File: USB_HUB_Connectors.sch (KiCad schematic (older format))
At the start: 86 parts, among them IC4 AP22652W6-7, J10 E8124-015-01, J11 E8124-015-01, U15 USB57442G, Y2 ABM8G-25.000MHZ-B4Y-T

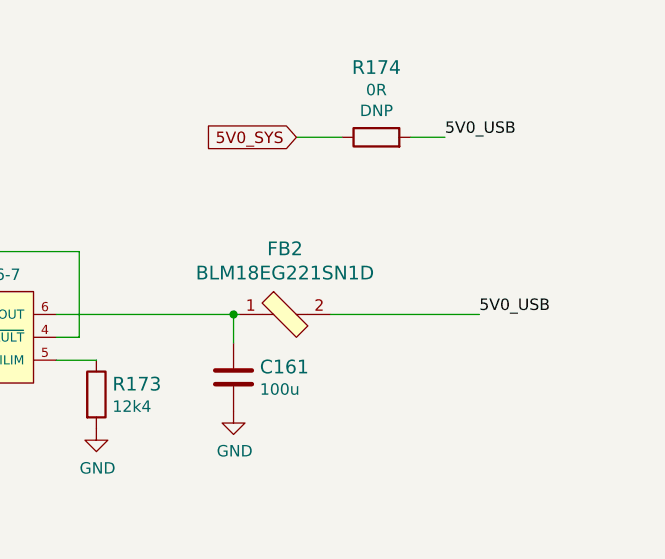
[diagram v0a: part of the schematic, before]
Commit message: Connecting LT9611
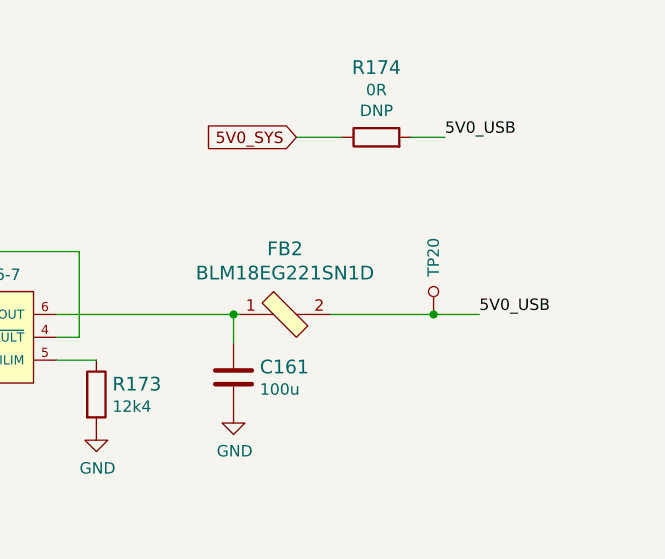
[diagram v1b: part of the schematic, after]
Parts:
- added TP20: TP_SMD_0_75MM, sc606-baseboard-footprints:Testpoint_smd_0_75mm, symbol sc606-baseboard:TP_SMD_0_75MM
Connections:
- net 5V0_USB: now also TP20.1
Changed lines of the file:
@@
 5V0_USB
 Wire Wire Line
-	15225 1925 14575 1925
+	15225 1925 15025 1925
 $Comp
 L sc606-baseboard:R_200k_0402 R?
@@
 P 12400 7400
 AR Path="/61F60810/620C24E5" Ref="#PWR?"  Part="1"
-AR Path="/63348E64/620C24E5" Ref="#PWR?"  Part="1"
-F 0 "#PWR?" H 12400 7150 50  0001 C CNN
+AR Path="/63348E64/620C24E5" Ref="#PWR0199"  Part="1"
+F 0 "#PWR0199" H 12400 7150 50  0001 C CNN
 F 1 "GND" H 12405 7227 50  0000 C CNN
 F 2 "" H 12400 7400 50  0001 C CNN
@@
 P 4550 8300
 AR Path="/61F60810/620CB62E" Ref="#PWR?"  Part="1"
-AR Path="/63348E64/620CB62E" Ref="#PWR?"  Part="1"
-F 0 "#PWR?" H 4550 8050 50  0001 C CNN
+AR Path="/63348E64/620CB62E" Ref="#PWR0200"  Part="1"
+F 0 "#PWR0200" H 4550 8050 50  0001 C CNN
 F 1 "GND" H 4555 8127 50  0000 C CNN
 F 2 "" H 4550 8300 50  0001 C CNN
@@
 	-1   0    0    -1
 $EndComp
+$Comp
+L sc606-baseboard:TP_SMD_0_75MM TP20
+U 1 1 621ACE00
+P 15025 1825
+F 0 "TP20" V 15025 1675 50  0000 C CNN
+F 1 "TP_SMD_0_75MM" H 15025 1725 50  0001 C CNN
+F 2 "sc606-baseboard-footprints:Testpoint_smd_0_75mm" H 15225 2025 60  0001 L CNN
+F 3 "" H 15225 2125 60  0001 L CNN
+	1    15025 1825
+	-1   0    0    1
+$EndComp
+Connection ~ 15025 1925
+Wire Wire Line
+	15025 1925 14575 1925
 $EndSCHEMATC

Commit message: Corrected power supplies. Change of TP to 1,5mm
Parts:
- TP18, TP19, TP20, TP23, TP24: value TP_SMD_0_75MM -> TP_SMD_1_5MM; footprint sc606-baseboard-footprints:Testpoint_smd_0_75mm -> sc606-baseboard-footprints:TP-R-1.5
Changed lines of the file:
@@
 P 11300 6600
 F 0 "TP23" V 11300 6450 50  0000 C CNN
-F 1 "TP_SMD_0_75MM" H 11300 6500 50  0001 C CNN
-F 2 "sc606-baseboard-footprints:Testpoint_smd_0_75mm" H 11500 6800 60  0001 L CNN
+F 1 "TP_SMD_1_5MM" H 11300 6500 50  0001 C CNN
+F 2 "sc606-baseboard-footprints:TP-R-1.5" H 11500 6800 60  0001 L CNN
 F 3 "" H 11500 6900 60  0001 L CNN
 	1    11300 6600
@@
 P 13200 6300
 F 0 "TP24" V 13200 6200 50  0000 C CNN
-F 1 "TP_SMD_0_75MM" H 13200 6200 50  0001 C CNN
-F 2 "sc606-baseboard-footprints:Testpoint_smd_0_75mm" H 13400 6500 60  0001 L CNN
+F 1 "TP_SMD_1_5MM" H 13200 6200 50  0001 C CNN
+F 2 "sc606-baseboard-footprints:TP-R-1.5" H 13400 6500 60  0001 L CNN
 F 3 "" H 13400 6600 60  0001 L CNN
 	1    13200 6300
@@
 P 3450 7500
 F 0 "TP18" V 3450 7350 50  0000 C CNN
-F 1 "TP_SMD_0_75MM" H 3450 7400 50  0001 C CNN
-F 2 "sc606-baseboard-footprints:Testpoint_smd_0_75mm" H 3650 7700 60  0001 L CNN
+F 1 "TP_SMD_1_5MM" H 3450 7400 50  0001 C CNN
+F 2 "sc606-baseboard-footprints:TP-R-1.5" H 3650 7700 60  0001 L CNN
 F 3 "" H 3650 7800 60  0001 L CNN
 	1    3450 7500
@@
 P 5350 7200
 F 0 "TP19" V 5350 7100 50  0000 C CNN
-F 1 "TP_SMD_0_75MM" H 5350 7100 50  0001 C CNN
-F 2 "sc606-baseboard-footprints:Testpoint_smd_0_75mm" H 5550 7400 60  0001 L CNN
+F 1 "TP_SMD_1_5MM" H 5350 7100 50  0001 C CNN
+F 2 "sc606-baseboard-footprints:TP-R-1.5" H 5550 7400 60  0001 L CNN
 F 3 "" H 5550 7500 60  0001 L CNN
 	1    5350 7200
@@
 P 15025 1825
 F 0 "TP20" V 15025 1675 50  0000 C CNN
-F 1 "TP_SMD_0_75MM" H 15025 1725 50  0001 C CNN
-F 2 "sc606-baseboard-footprints:Testpoint_smd_0_75mm" H 15225 2025 60  0001 L CNN
+F 1 "TP_SMD_1_5MM" H 15025 1725 50  0001 C CNN
+F 2 "sc606-baseboard-footprints:TP-R-1.5" H 15225 2025 60  0001 L CNN
 F 3 "" H 15225 2125 60  0001 L CNN
 	1    15025 1825

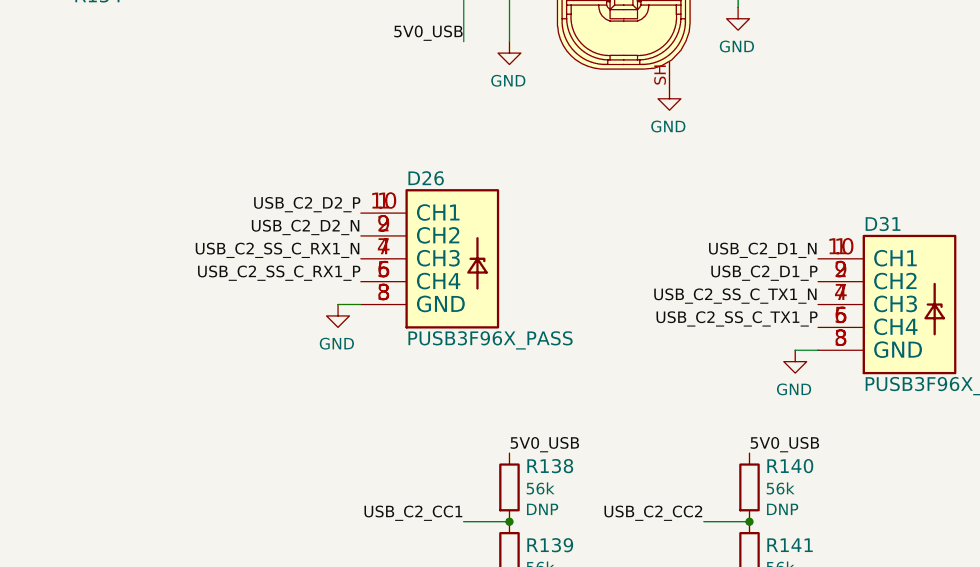
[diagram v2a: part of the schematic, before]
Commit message: Added schema for serial interface connectors
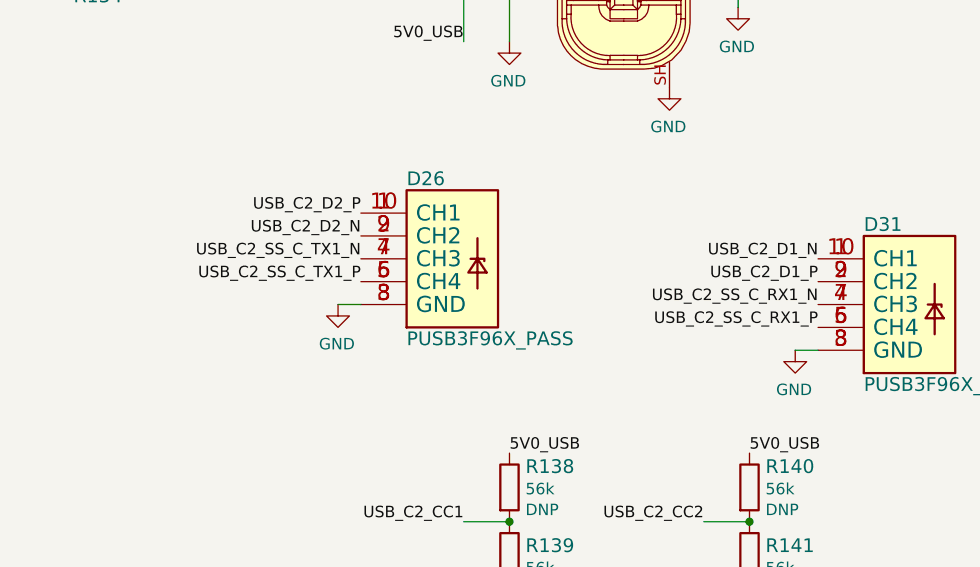
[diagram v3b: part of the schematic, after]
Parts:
- TP13, TP14, TP15, TP16, TP17: value TP_SMD_0_75MM-antmicroTestPoints -> TP_SMD_1_5MM; footprint sc606-baseboard-footprints:Testpoint_smd_0_75mm -> sc606-baseboard-footprints:TP-R-1.5
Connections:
- net USB_C2_SS_C_RX1_N: now also D31.4 (CH3), D31.7 (CH3); no longer D26.4 (CH3), D26.7 (CH3)
- net USB_C2_SS_C_RX1_P: now also D31.5 (CH4), D31.6 (CH4); no longer D26.5 (CH4), D26.6 (CH4)
- net USB_C2_SS_C_TX1_N: now also D26.4 (CH3), D26.7 (CH3); no longer D31.4 (CH3), D31.7 (CH3)
- net USB_C2_SS_C_TX1_P: now also D26.5 (CH4), D26.6 (CH4); no longer D31.5 (CH4), D31.6 (CH4)
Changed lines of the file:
@@
 AR Path="/63348E64/6336FA49" Ref="TP13"  Part="1"
 F 0 "TP13" H 1350 2047 50  0000 R CNN
-F 1 "TP_SMD_0_75MM-antmicroTestPoints" H 1400 1900 50  0001 C CNN
-F 2 "sc606-baseboard-footprints:Testpoint_smd_0_75mm" H 1600 2200 60  0001 L CNN
+F 1 "TP_SMD_1_5MM" H 1400 1900 50  0001 C CNN
+F 2 "sc606-baseboard-footprints:TP-R-1.5" H 1600 2200 60  0001 L CNN
 F 3 "" H 1600 2300 60  0001 L CNN
 	1    1400 2000
@@
 AR Path="/63348E64/635BD552" Ref="TP16"  Part="1"
 F 0 "TP16" V 2575 3125 50  0000 C CNN
-F 1 "TP_SMD_0_75MM-antmicroTestPoints" H 2600 2900 50  0001 C CNN
-F 2 "sc606-baseboard-footprints:Testpoint_smd_0_75mm" H 2800 3200 60  0001 L CNN
+F 1 "TP_SMD_1_5MM" H 2600 2900 50  0001 C CNN
+F 2 "sc606-baseboard-footprints:TP-R-1.5" H 2800 3200 60  0001 L CNN
 F 3 "" H 2800 3300 60  0001 L CNN
 	1    2600 3000
@@
 AR Path="/63348E64/635BDBB6" Ref="TP17"  Part="1"
 F 0 "TP17" V 2575 3325 50  0000 C CNN
-F 1 "TP_SMD_0_75MM-antmicroTestPoints" H 2600 3100 50  0001 C CNN
-F 2 "sc606-baseboard-footprints:Testpoint_smd_0_75mm" H 2800 3400 60  0001 L CNN
+F 1 "TP_SMD_1_5MM" H 2600 3100 50  0001 C CNN
+F 2 "sc606-baseboard-footprints:TP-R-1.5" H 2800 3400 60  0001 L CNN
 F 3 "" H 2800 3500 60  0001 L CNN
 	1    2600 3200
@@
 AR Path="/63348E64/635CBB18" Ref="TP14"  Part="1"
 F 0 "TP14" H 2425 2750 50  0000 R CNN
-F 1 "TP_SMD_0_75MM-antmicroTestPoints" H 2450 2700 50  0001 C CNN
-F 2 "sc606-baseboard-footprints:Testpoint_smd_0_75mm" H 2650 3000 60  0001 L CNN
+F 1 "TP_SMD_1_5MM" H 2450 2700 50  0001 C CNN
+F 2 "sc606-baseboard-footprints:TP-R-1.5" H 2650 3000 60  0001 L CNN
 F 3 "" H 2650 3100 60  0001 L CNN
 	1    2450 2800
@@
 AR Path="/63348E64/635CC318" Ref="TP15"  Part="1"
 F 0 "TP15" H 2325 2950 50  0000 L CNN
-F 1 "TP_SMD_0_75MM-antmicroTestPoints" H 2450 2900 50  0001 C CNN
-F 2 "sc606-baseboard-footprints:Testpoint_smd_0_75mm" H 2650 3200 60  0001 L CNN
+F 1 "TP_SMD_1_5MM" H 2450 2900 50  0001 C CNN
+F 2 "sc606-baseboard-footprints:TP-R-1.5" H 2650 3200 60  0001 L CNN
 F 3 "" H 2650 3300 60  0001 L CNN
 	1    2450 3000
@@
 Text Label 13050 8150 2    50   ~ 0
 USB_C2_D1_N
-Text Label 11050 8150 2    50   ~ 0
+Text Label 13050 8350 2    50   ~ 0
 USB_C2_SS_C_RX1_N
-Text Label 11050 8250 2    50   ~ 0
+Text Label 13050 8450 2    50   ~ 0
 USB_C2_SS_C_RX1_P
 Wire Wire Line
@@
 	1    0    0    -1
 $EndComp
-Text Label 13050 8450 2    50   ~ 0
+Text Label 11050 8250 2    50   ~ 0
 USB_C2_SS_C_TX1_P
-Text Label 13050 8350 2    50   ~ 0
+Text Label 11050 8150 2    50   ~ 0
 USB_C2_SS_C_TX1_N
 $Comp

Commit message: Debug connector moved away from chip. Corrected wifi antenna ground plane. Added arcs on GNSS and WiFi tracks
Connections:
- net 5V0_USB: now also C103.1, C139.1; no longer C103.2, C139.2
- net GND: now also C103.2, C139.2; no longer C103.1, C139.1
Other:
- note added: "ESD Protection"
- note added: "USB-C Connectors"
- note added: "USB-C connector 1"
- note added: "USB-C connector 2"
- note removed: "USB-C connector"
- moved on the sheet: C102, C103, C118, C119, C120, C121, C122, C123, C124, C125, C126, C127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

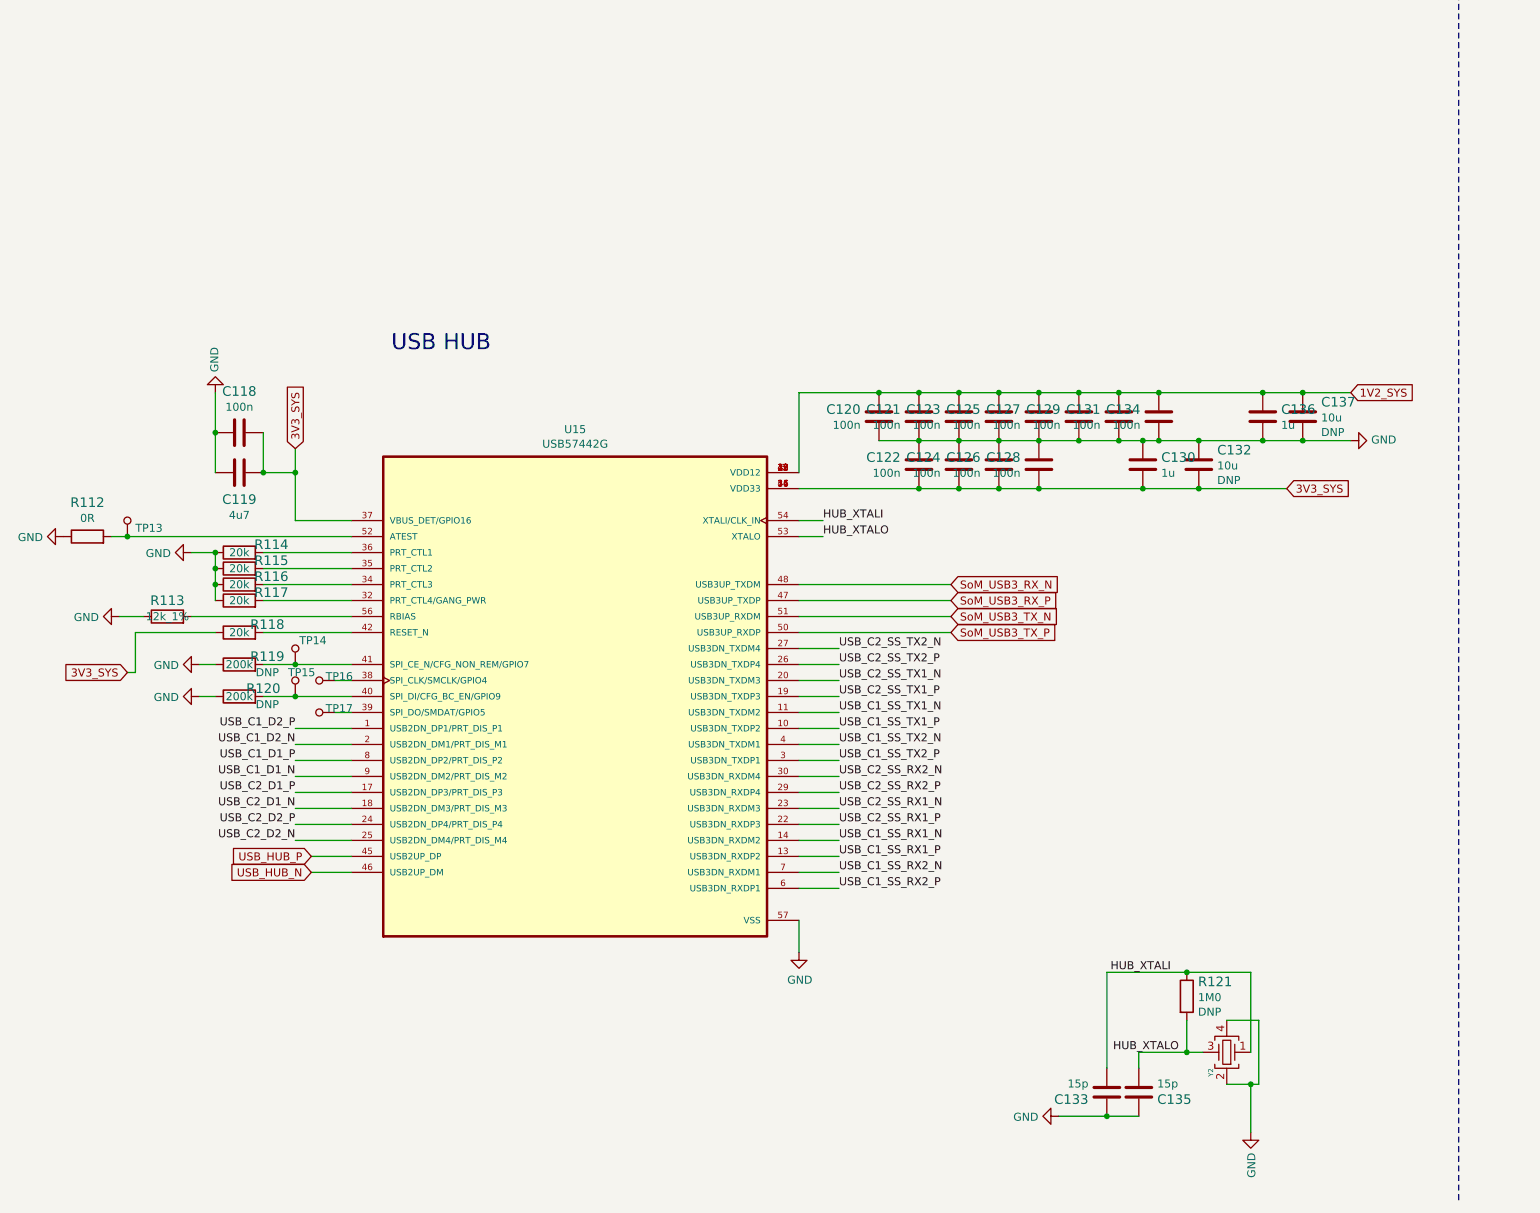
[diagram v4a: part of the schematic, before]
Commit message: Schematic cleanup-USB HUB
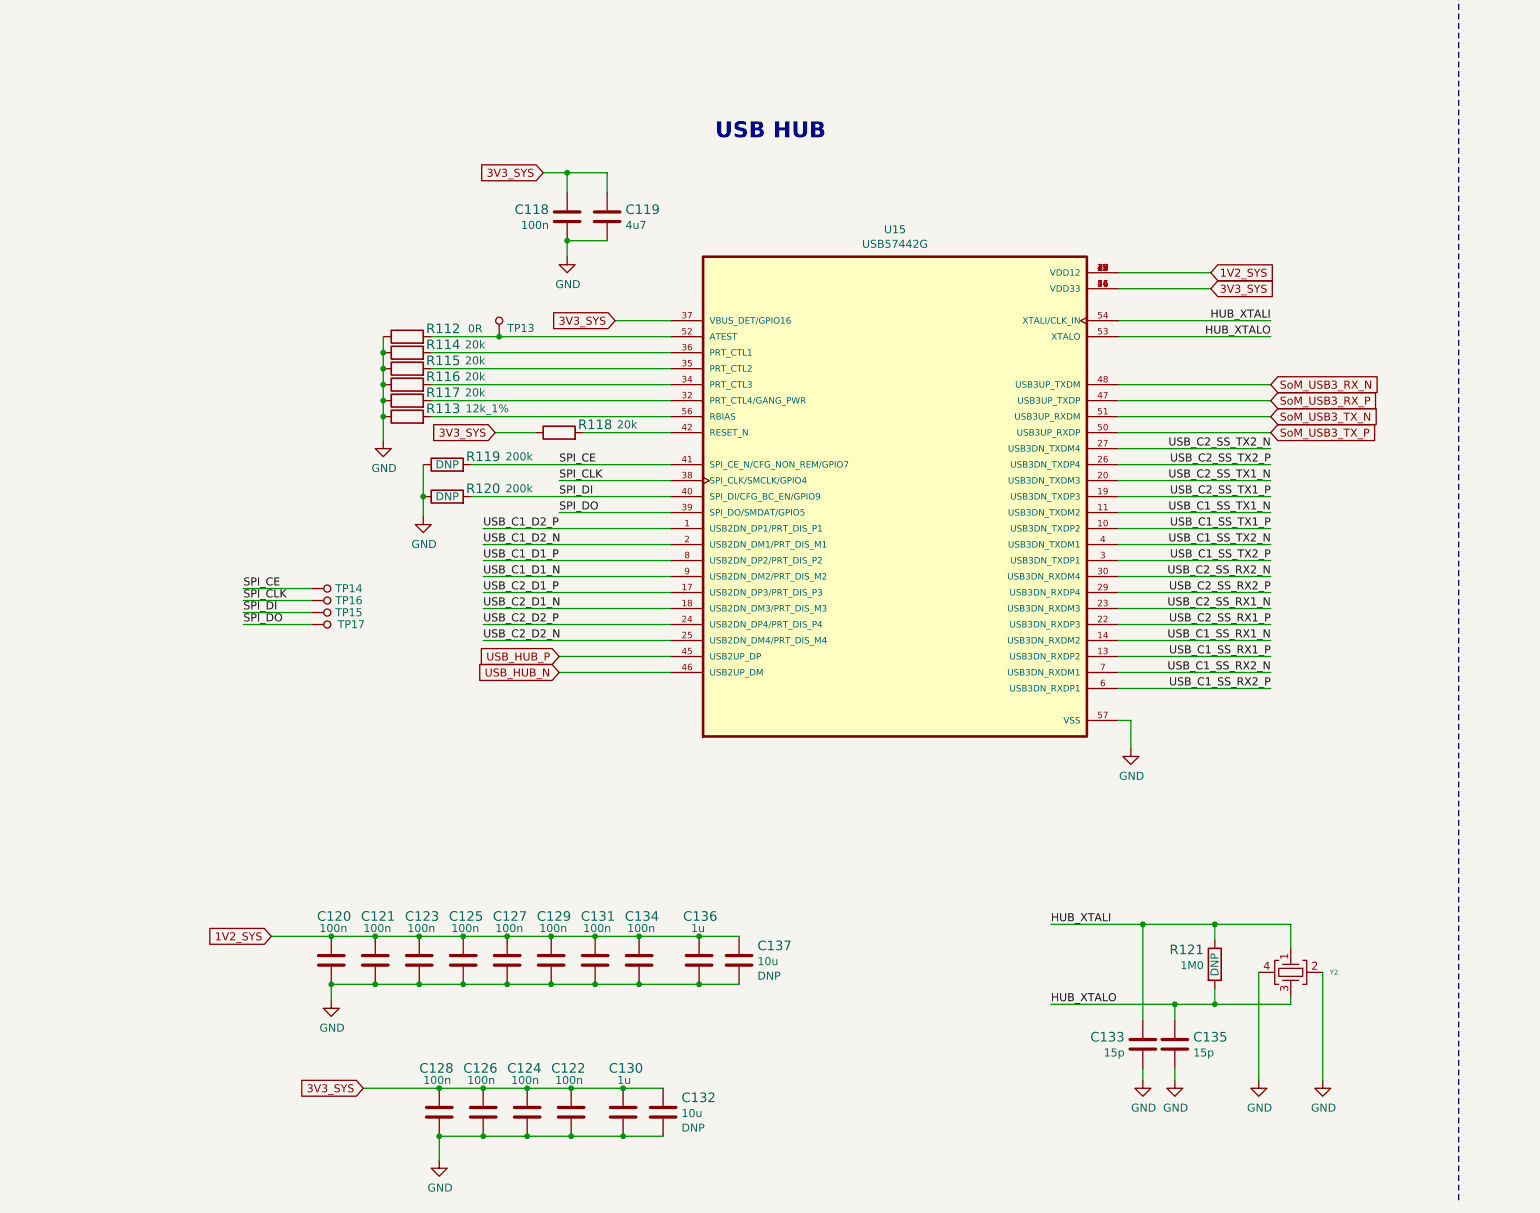
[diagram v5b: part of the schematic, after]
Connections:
- net SPI_CLK: now reaches TP16.1, U15.38 (SPI_CLK/SMCLK/GPIO4)
- net SPI_DO: now reaches TP17.1, U15.39 (SPI_DO/SMDAT/GPIO5)
- net SPI_DI: now reaches R120.2, TP15.1, U15.40 (SPI_DI/CFG_BC_EN/GPIO9)
- net SPI_CE: now reaches R119.2, TP14.1, U15.41 (SPI_CE_N/CFG_NON_REM/GPIO7)
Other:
- moved on the sheet: C118, C119, C120, C121, C122, C123, C124, C125, C126, C127, C128, C129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

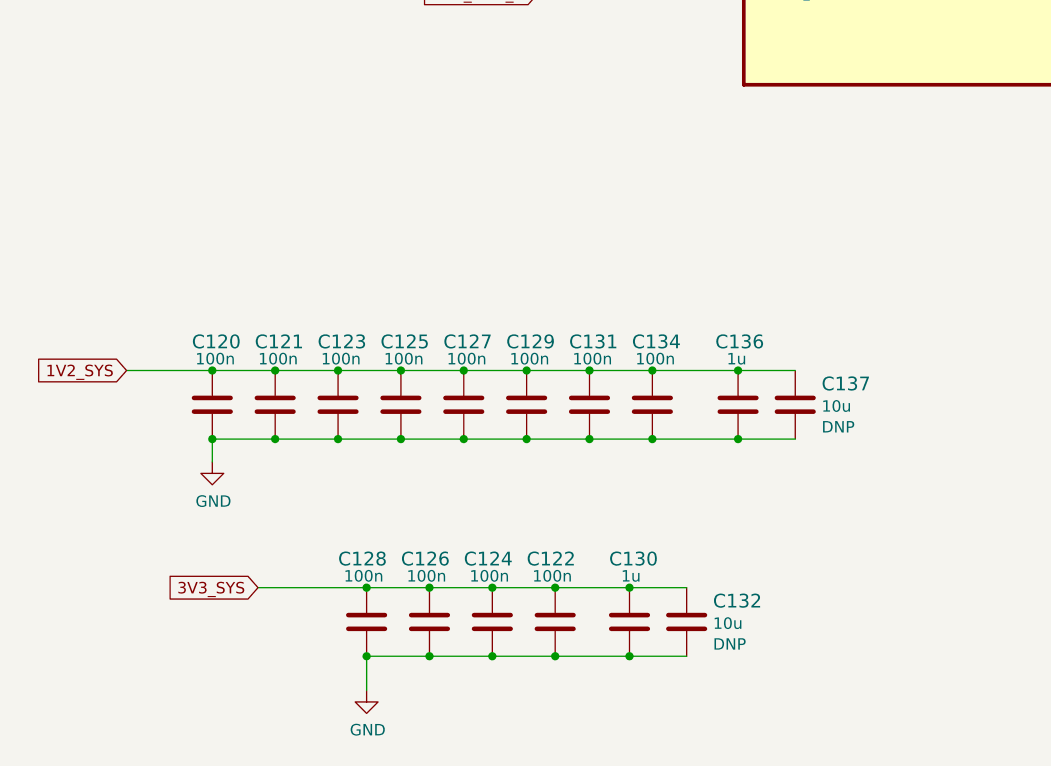
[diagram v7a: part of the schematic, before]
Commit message: Update the sch signage, remove redundant sheets
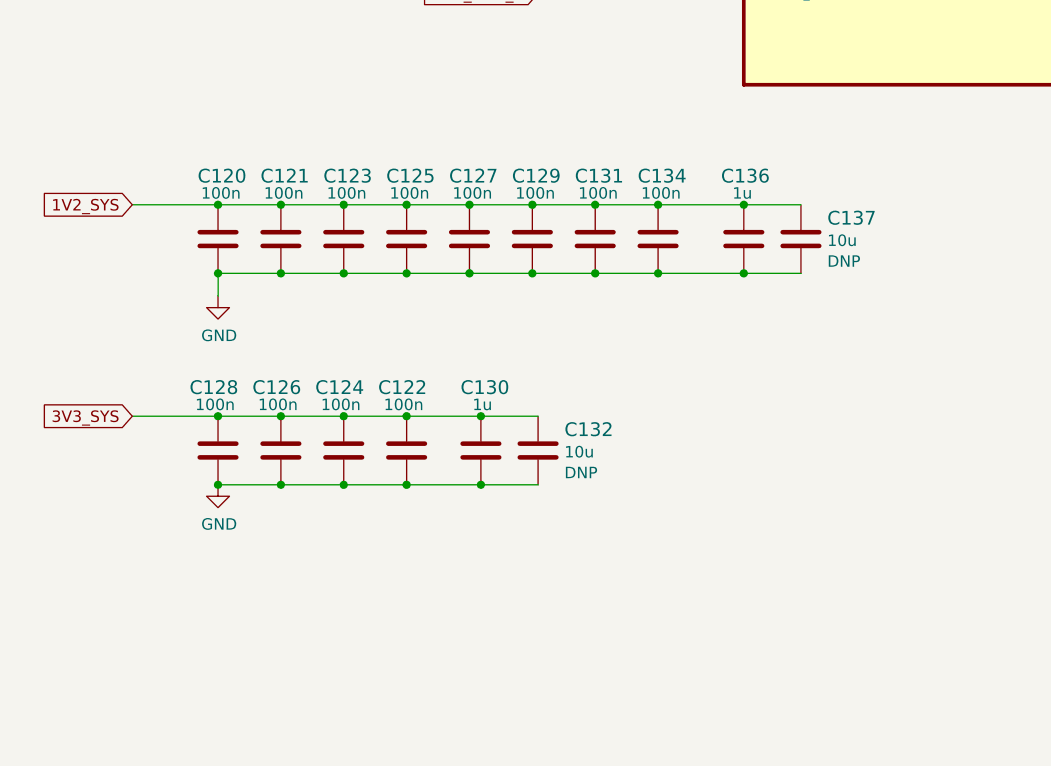
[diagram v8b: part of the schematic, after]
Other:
- moved on the sheet: C120, C121, C122, C123, C124, C125, C126, C127, C128, C129, C130, C131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
